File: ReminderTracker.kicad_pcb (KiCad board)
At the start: 2 copper layers, 92 x 150 mm, 24 parts, among them J1 External RTC, SW1 SW_Push, SW2 SW_Push, SW3 SW_Push, SW4 SW_Push, SW5 SW_Push, SW6 SW_Push, U1 XIAO-ESP32-C3-DIP

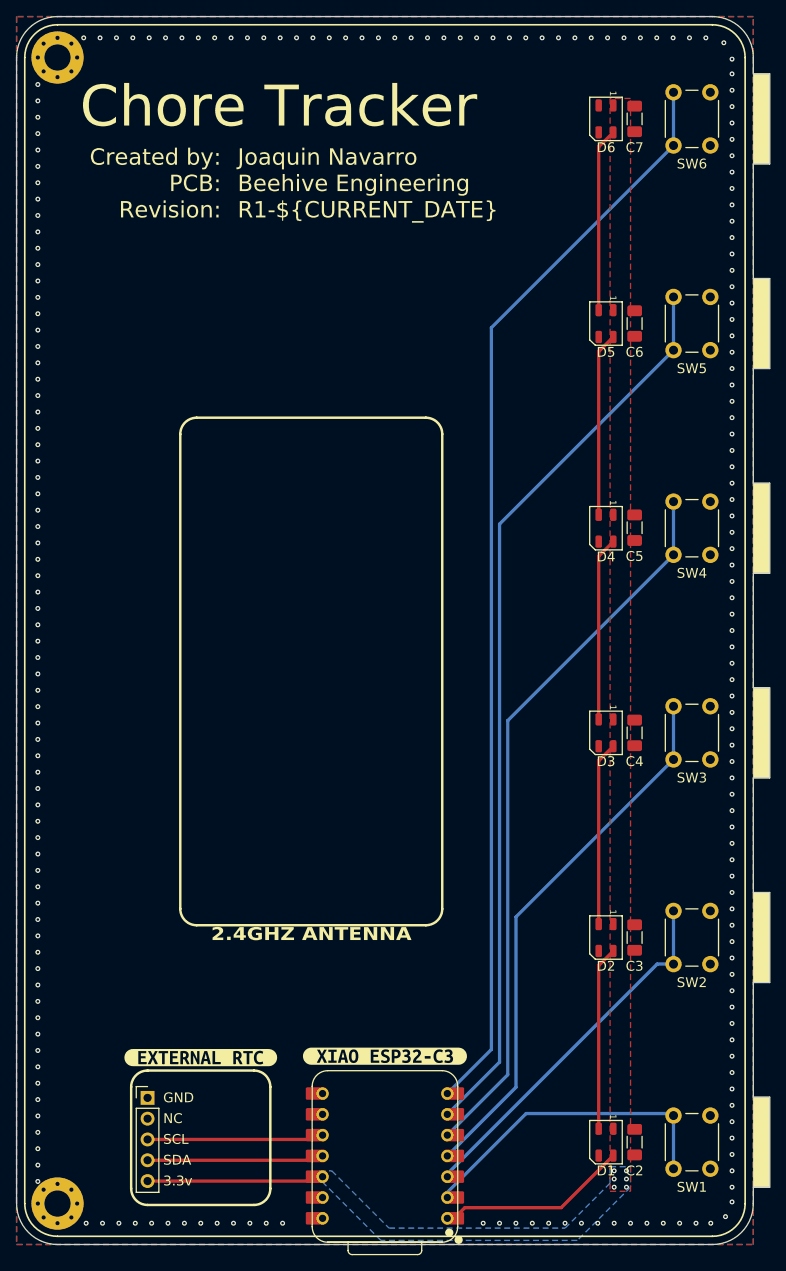
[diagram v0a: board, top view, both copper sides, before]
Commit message: R2
Fix title
Added antenna cutout
Renamed to Task Tracker
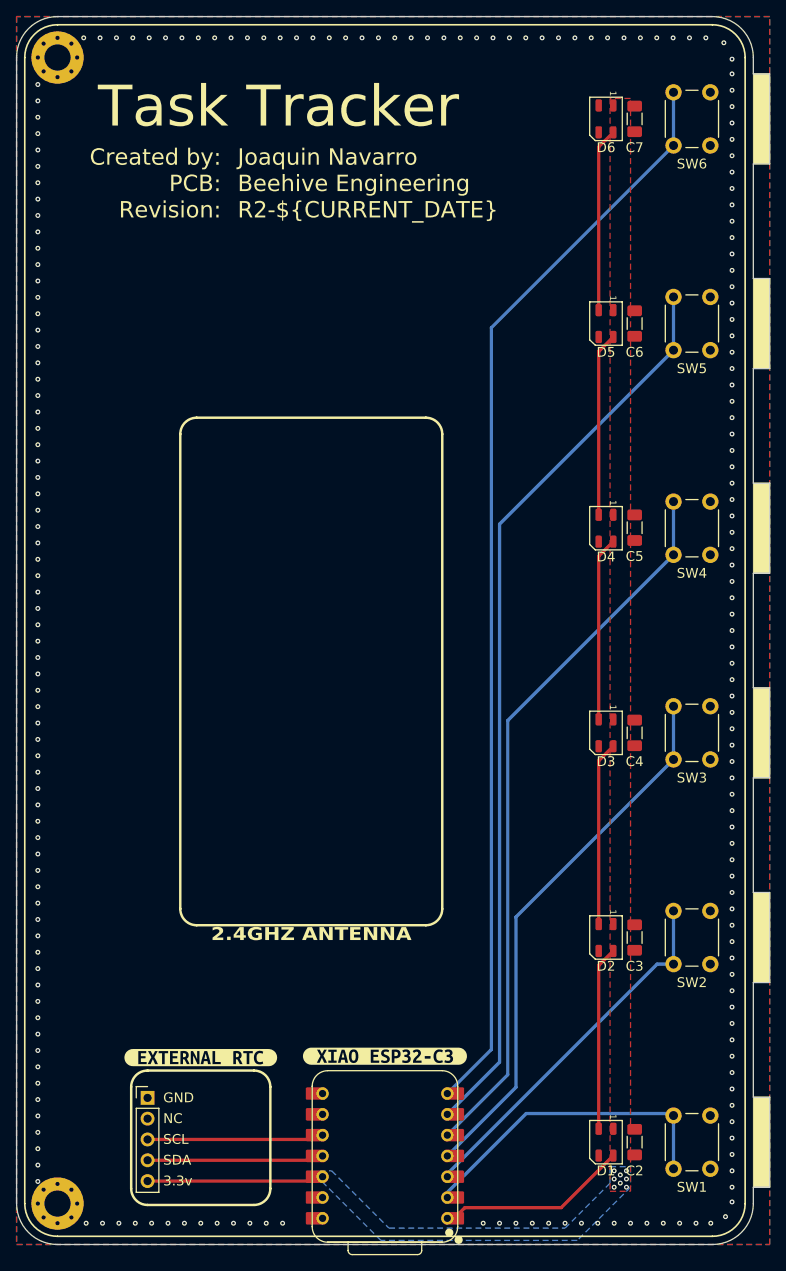
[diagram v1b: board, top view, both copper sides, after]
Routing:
- net +3.3V: vias 6 -> 8
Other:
- board text added: "Task Tracker"
- board text removed: "Chore Tracker"

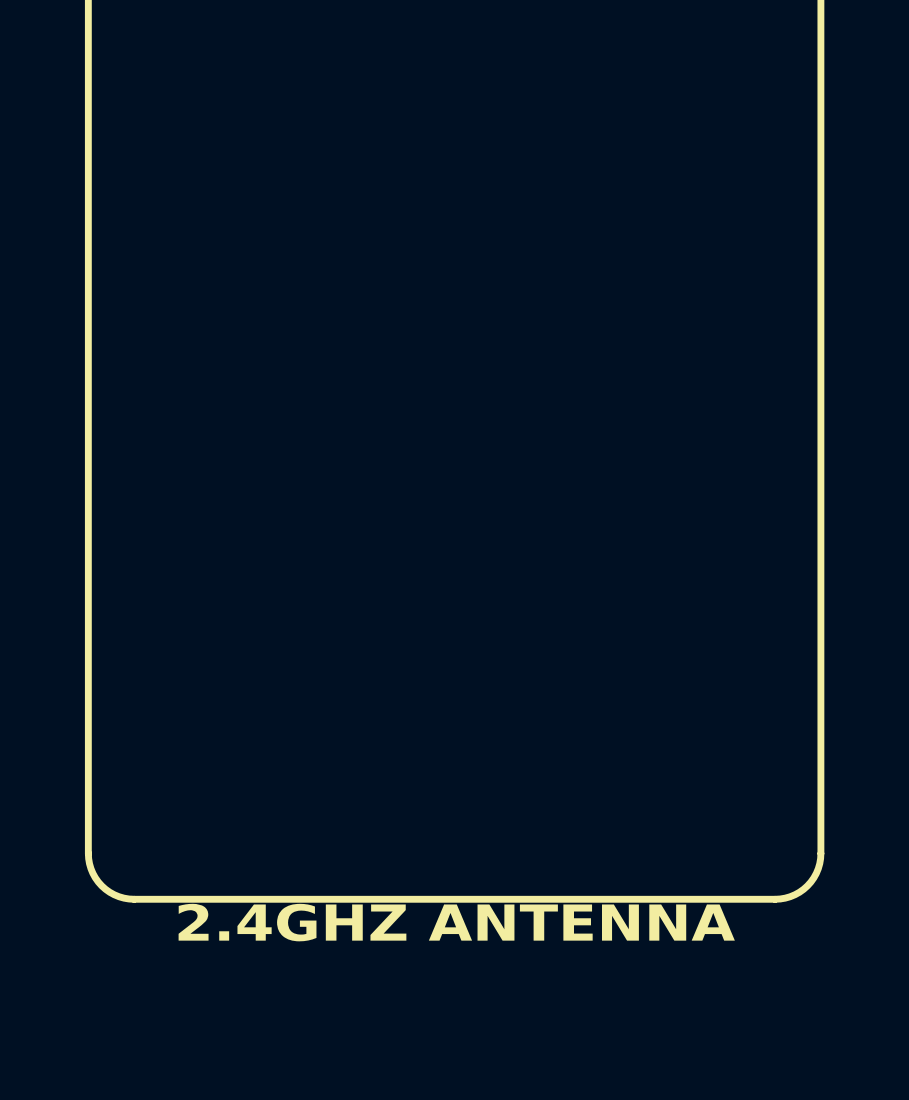
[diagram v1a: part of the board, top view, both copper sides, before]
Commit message: Antenna visual fixes
- added silkscreen band around backside of antenna cutout
- swapped antenna text for kiBuzzard labels
- rounded antenna keepout and mask removal area
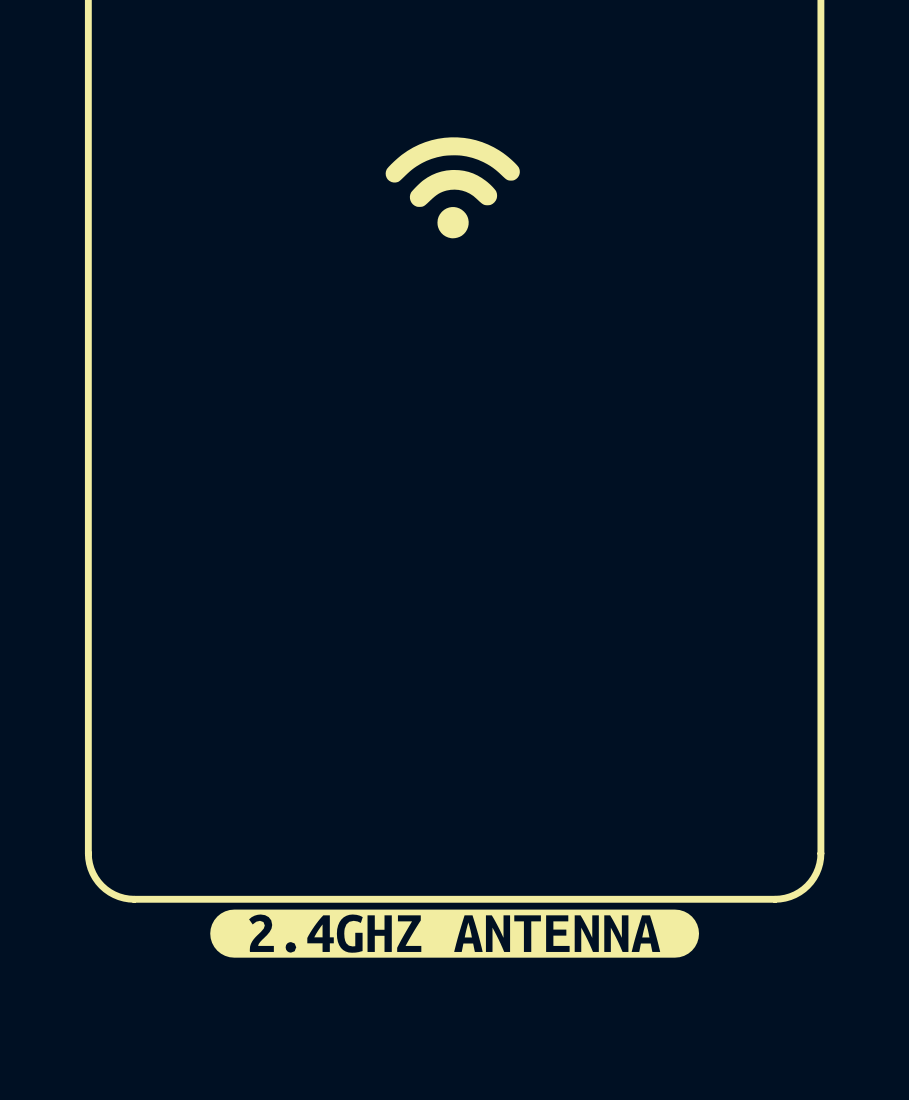
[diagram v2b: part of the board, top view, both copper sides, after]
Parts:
- added ?: , clipboard:a3d0cb5d-562f-47cd-b0bb-de1c63e23321, F.Cu at (91.0, 110.0)
- added G***: LOGO, LOGO, B.Cu at (91.0, 111.0)
- added kibuzzard-69C179A5: G***, kibuzzard-69C179A5, F.Cu at (91.0, 142.5)
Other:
- board text removed: "2.4GHZ ANTENNA"
